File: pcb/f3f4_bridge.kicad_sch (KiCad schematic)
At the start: 24 parts, among them J1 Screw_Terminal_01x02, J2 USB_C_Receptacle_USB2.0_14P, J3 Conn_01x05_Pin, J4 USB_B_Micro, U1 THVD8000, U2 STM32F042K6Ux, U3 TLV70033_SOT23-5

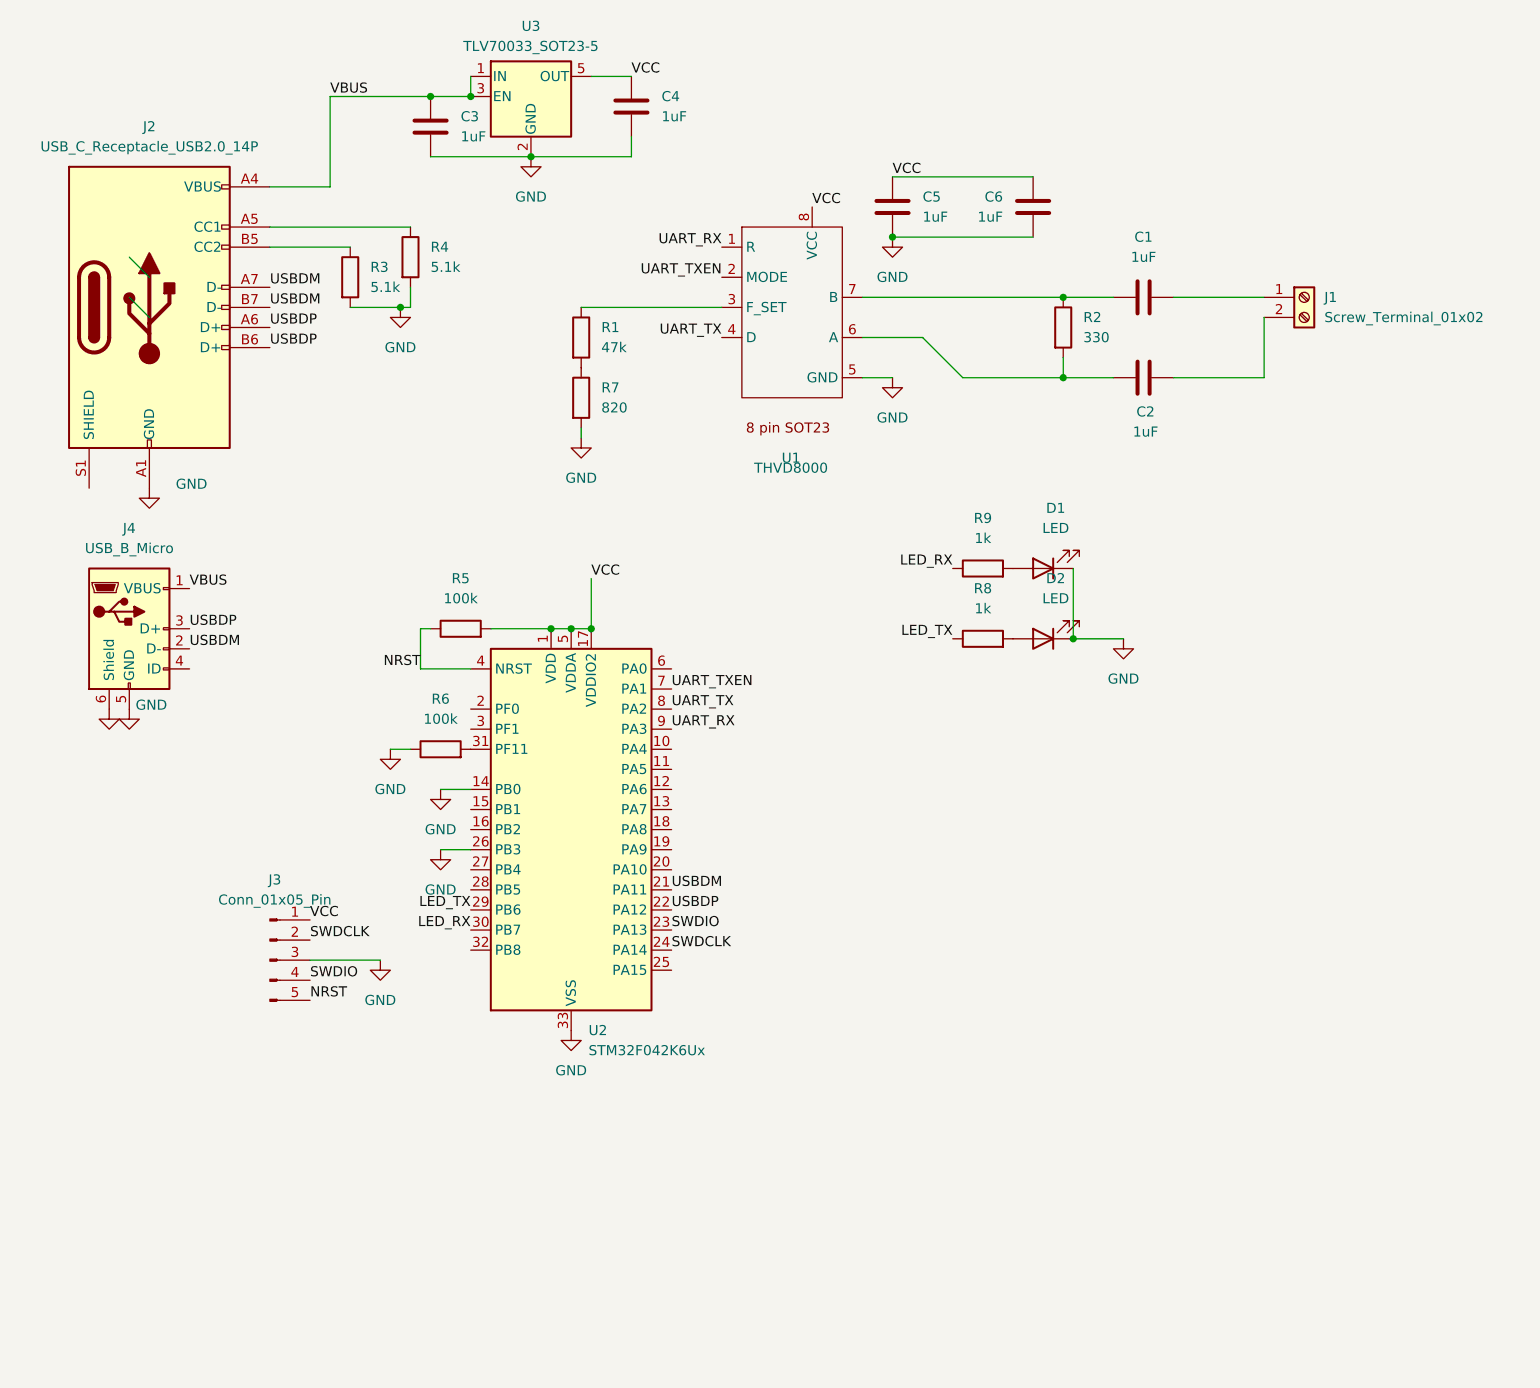
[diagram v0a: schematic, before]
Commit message: add back to STM32 bootloader (masserase) add rule to flash using dfu-util fix led lighting
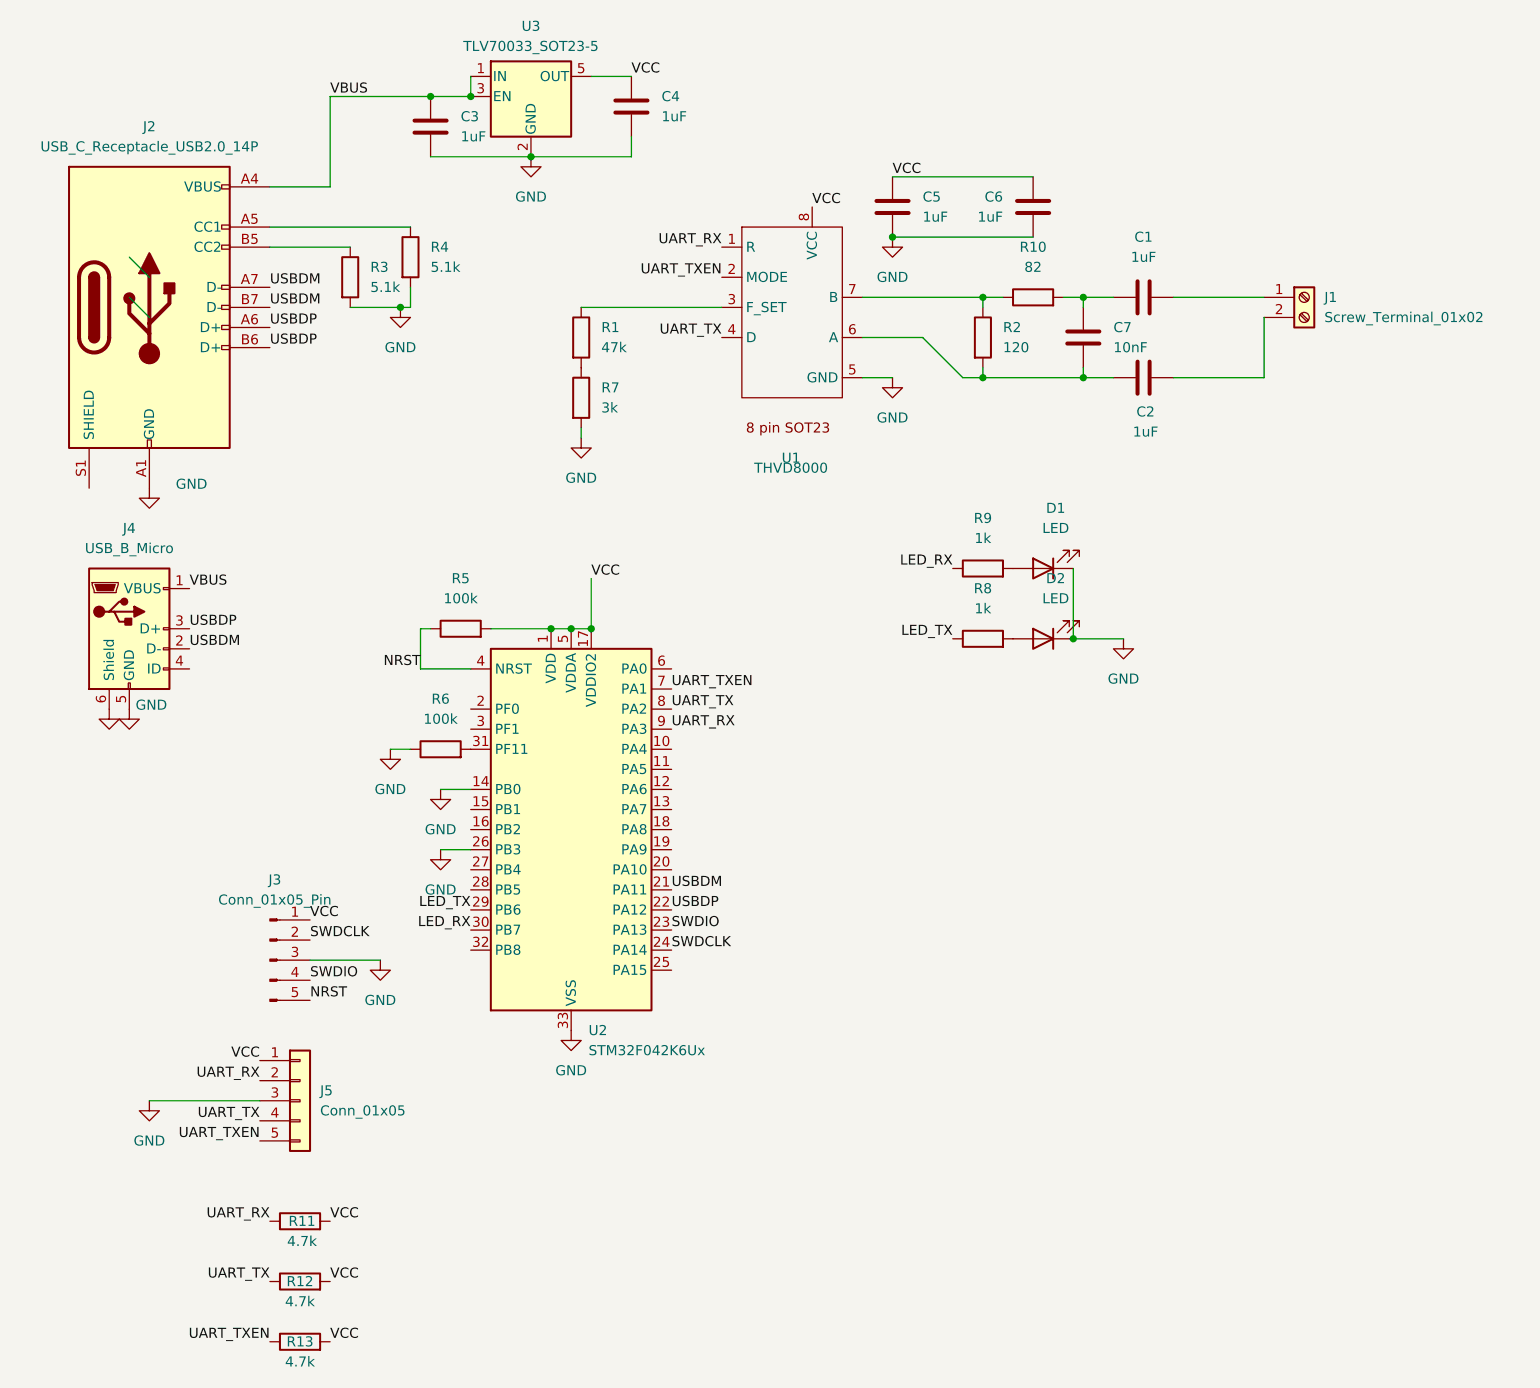
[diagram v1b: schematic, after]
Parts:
- added C7: 10nF, Capacitor_SMD:C_0603_1608Metric, symbol Device:C
- added J5: Conn_01x05, Connector_PinHeader_2.54mm:PinHeader_1x05_P2.54mm_Vertical, symbol Connector_Generic:Conn_01x05
- added R10: 82, Resistor_SMD:R_0603_1608Metric, symbol Device:R
- added R11, R12, R13: 4.7k, Resistor_SMD:R_0603_1608Metric, symbol Device:R
- C1, C2, C3, C4, C5, C6: LCSC (none) -> C15849
- D1, D2: LCSC (none) -> C2286
- J1: LCSC (none) -> C709041
- J2: LCSC (none) -> C2765186
- J3: LCSC (none) -> C492404
- R1: LCSC (none) -> C25819
- R2: value 330 -> 120; LCSC (none) -> C22787
- R3, R4: LCSC (none) -> C23186
- R5, R6: LCSC (none) -> C25803
- R7: value 820 -> 3k; LCSC (none) -> C4211
- R8, R9: LCSC (none) -> C21190
- U1: LCSC (none) -> C2848812
- U2: LCSC (none) -> C2053439
- U3: LCSC (none) -> C5884123
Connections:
- net GND: now also J5.3 (Pin_3)
- net UART_RX: now also J5.2 (Pin_2), R11.1
- net UART_TX: now also J5.4 (Pin_4), R12.1
- net UART_TXEN: now also J5.5 (Pin_5), R13.1
- net VCC: now also J5.1 (Pin_1), R11.2, R12.2, R13.2
- net at R2.1, U1.7 (B): now also R10.1; no longer C1.1
- net at C2.1, R2.2, U1.6 (A): now also C7.1
- new net: C1.1, C7.2, R10.2
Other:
- moved on the sheet: R2

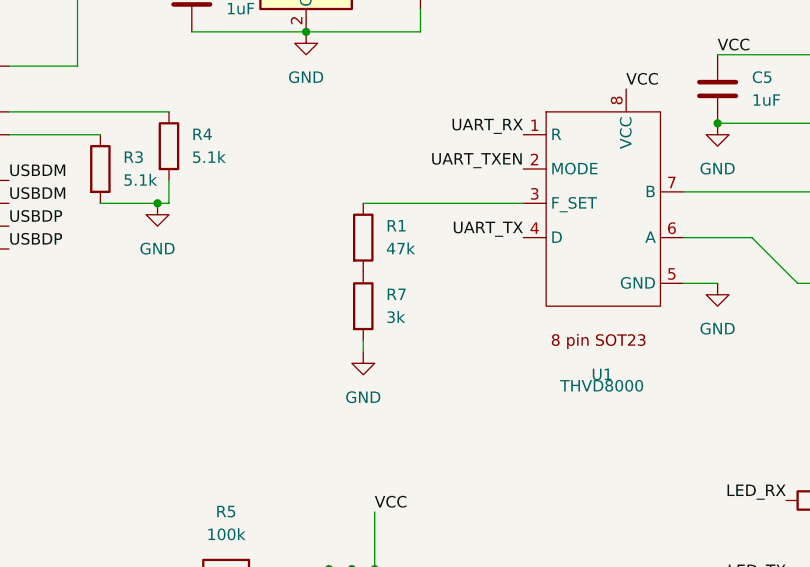
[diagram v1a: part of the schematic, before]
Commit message: fix invalid inverted rx and tx leds
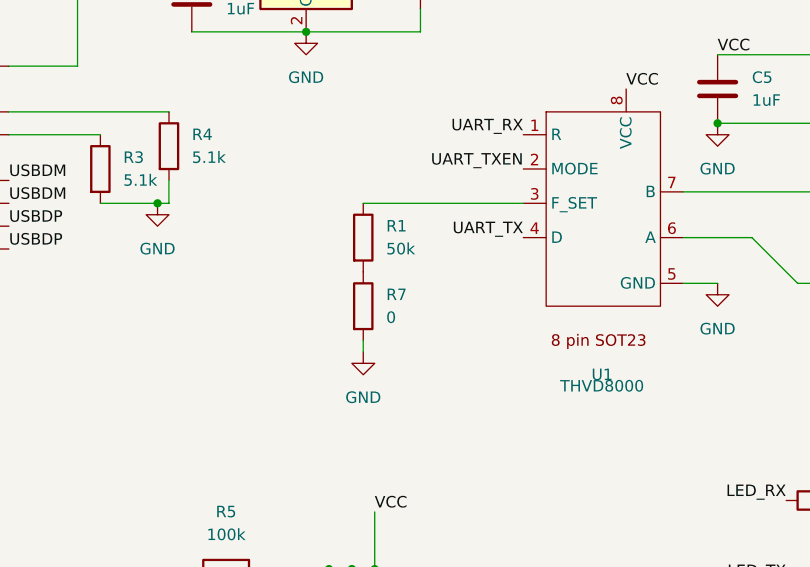
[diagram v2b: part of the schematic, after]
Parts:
- R1: value 47k -> 50k
- R7: value 3k -> 0
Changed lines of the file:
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@@
 			)
 		)
-		(property "Value" "3k"
+		(property "Value" "0"
 			(at 88.9 64.7699 0)
 			(effects
@@
 			)
 		)
-		(property "Value" "47k"
+		(property "Value" "50k"
 			(at 88.9 57.1499 0)
 			(effects
